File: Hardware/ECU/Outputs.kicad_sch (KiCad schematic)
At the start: 25 parts, among them IC2 ZXMS6006DT8, IC3 ZXMS6006DT8, IC4 ZXMS6006DT8

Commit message: modified:   .gitmodules 	modified:   Hardware/ECU/Comms.kicad_sch 	modified:   Hardware/ECU/ECU.kicad_pcb 	modified:   Hardware/ECU/ECU.kicad_pro 	modified:   Hardware/ECU/ECU.kicad_sch 	modified:   Hardware/ECU/Inputs.kicad_sch 	modified:   Hardware/ECU/Outputs.kicad_sch 	modified:   Hardware/ECU/fp-info-cache 	modified:   Hardware/ECU/fp-lib-table 	deleted:    docs/ECU info.url 	modified:   tune/Hayabusa-R1/CurrentTune.msq 	modified:   tune/Hayabusa-R1/projectCfg/project.properties 	modified:   tune/Hayabusa-R1/projectCfg/project.properties.bkup 	Hardware/ECU/ECU-backups/ECU-2024-11-07_084642.zip 	Hardware/ECU/ECU-backups/ECU-2024-11-07_091524.zip 	Hardware/ECU/ECU-backups/ECU-2024-11-07_094217.zip 	Hardware/ECU/ECU-backups/ECU-2024-11-07_120300.zip 	Hardware/ECU/ECU-backups/ECU-2024-11-08_085235.zip 	Hardware/ECU/ECU-backups/ECU-2024-11-08_091401.zip 	Hardware/ECU/ECU-backups/ECU-2024-11-08_103901.zip 	Hardware/ECU/docs/ 	Hardware/ECU/lib/2999/ 	Hardware/ECU/lib/IC_Automotive/IC_Automotive.pretty/BAT_2999.kicad_mod 	Hardware/ECU/lib/IC_Automotive/IC_Automotive.pretty/ZXMS6006DT8TA.kicad_mod 	Hardware/ECU/lib/ZXMS6006DT8TA/ 	Hardware/ECU/lib/teensy_library/ 	Hardware/ECU/output.pdf 	Hardware/ECU/report.txt 	docs/Speeduino_manual.pdf 	docs/Speeduino_manual.pdf:Zone.Identifier 	tune/Hayabusa-R1/dashboard/lambdaTable1Map.dash 	tune/Hayabusa-R1/dashboard/stagingMap.dash 	tune/TunerStudioAppDebug.txt
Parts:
- IC2, IC3, IC4: footprint IC_Automotive:Diodes_SM8 -> ZXMS6006DT8TA:SOT153P700X170-8N
- R53, R54, R55, R56, R58, R59, R60, R61, R62, R63, R64, R65: footprint Resistor_SMD:R_0805_2012Metric_Pad1.15x1.40mm_HandSolder -> Resistor_SMD:R_0805_2012Metric_Pad1.20x1.40mm_HandSolder
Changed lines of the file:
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@@
 			)
 		)
-		(property "Footprint" "Resistor_SMD:R_0805_2012Metric_Pad1.15x1.40mm_HandSolder"
+		(property "Footprint" "Resistor_SMD:R_0805_2012Metric_Pad1.20x1.40mm_HandSolder"
 			(at 194.818 110.49 90)
 			(effects
@@
 			)
 		)
-		(property "Footprint" "Resistor_SMD:R_0805_2012Metric_Pad1.15x1.40mm_HandSolder"
+		(property "Footprint" "Resistor_SMD:R_0805_2012Metric_Pad1.20x1.40mm_HandSolder"
 			(at 186.69 116.332 90)
 			(effects
@@
 			)
 		)
-		(property "Footprint" "Resistor_SMD:R_0805_2012Metric_Pad1.15x1.40mm_HandSolder"
+		(property "Footprint" "Resistor_SMD:R_0805_2012Metric_Pad1.20x1.40mm_HandSolder"
 			(at 50.038 57.15 90)
 			(effects
@@
 			)
 		)
-		(property "Footprint" "Resistor_SMD:R_0805_2012Metric_Pad1.15x1.40mm_HandSolder"
+		(property "Footprint" "Resistor_SMD:R_0805_2012Metric_Pad1.20x1.40mm_HandSolder"
 			(at 194.818 130.81 90)
 			(effects
@@
 			)
 		)
-		(property "Footprint" "IC_Automotive:Diodes_SM8"
+		(property "Footprint" "ZXMS6006DT8TA:SOT153P700X170-8N"
 			(at 236.22 41.91 0)
 			(effects
@@
 			)
 		)
-		(property "Footprint" "Resistor_SMD:R_0805_2012Metric_Pad1.15x1.40mm_HandSolder"
+		(property "Footprint" "Resistor_SMD:R_0805_2012Metric_Pad1.20x1.40mm_HandSolder"
 			(at 41.91 42.672 90)
 			(effects
@@
 			)
 		)
-		(property "Footprint" "Resistor_SMD:R_0805_2012Metric_Pad1.15x1.40mm_HandSolder"
+		(property "Footprint" "Resistor_SMD:R_0805_2012Metric_Pad1.20x1.40mm_HandSolder"
 			(at 196.088 36.83 90)
 			(effects
@@
 			)
 		)
-		(property "Footprint" "IC_Automotive:Diodes_SM8"
+		(property "Footprint" "ZXMS6006DT8TA:SOT153P700X170-8N"
 			(at 234.95 115.57 0)
 			(effects
@@
 			)
 		)
-		(property "Footprint" "Resistor_SMD:R_0805_2012Metric_Pad1.15x1.40mm_HandSolder"
+		(property "Footprint" "Resistor_SMD:R_0805_2012Metric_Pad1.20x1.40mm_HandSolder"
 			(at 41.91 47.752 90)
 			(effects
@@
 			)
 		)
-		(property "Footprint" "Resistor_SMD:R_0805_2012Metric_Pad1.15x1.40mm_HandSolder"
+		(property "Footprint" "Resistor_SMD:R_0805_2012Metric_Pad1.20x1.40mm_HandSolder"
 			(at 187.96 42.672 90)
 			(effects
@@
 			)
 		)
-		(property "Footprint" "Resistor_SMD:R_0805_2012Metric_Pad1.15x1.40mm_HandSolder"
+		(property "Footprint" "Resistor_SMD:R_0805_2012Metric_Pad1.20x1.40mm_HandSolder"
 			(at 50.038 36.83 90)
 			(effects
@@
 			)
 		)
-		(property "Footprint" "IC_Automotive:Diodes_SM8"
+		(property "Footprint" "ZXMS6006DT8TA:SOT153P700X170-8N"
 			(at 90.17 41.91 0)
 			(effects
@@
 			)
 		)
-		(property "Footprint" "Resistor_SMD:R_0805_2012Metric_Pad1.15x1.40mm_HandSolder"
+		(property "Footprint" "Resistor_SMD:R_0805_2012Metric_Pad1.20x1.40mm_HandSolder"
 			(at 186.69 121.412 90)
 			(effects
@@
 			)
 		)
-		(property "Footprint" "Resistor_SMD:R_0805_2012Metric_Pad1.15x1.40mm_HandSolder"
+		(property "Footprint" "Resistor_SMD:R_0805_2012Metric_Pad1.20x1.40mm_HandSolder"
 			(at 196.088 57.15 90)
 			(effects
@@
 			)
 		)
-		(property "Footprint" "Resistor_SMD:R_0805_2012Metric_Pad1.15x1.40mm_HandSolder"
+		(property "Footprint" "Resistor_SMD:R_0805_2012Metric_Pad1.20x1.40mm_HandSolder"
 			(at 187.96 47.752 90)
 			(effects

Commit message: PCB
Platine Vernetzt
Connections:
- net GND: now also R55.1; no longer R55.2
- net at IC2.1 (INPUT_1), R53.1: now also R55.2; no longer R55.1
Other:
- moved on the sheet: R55
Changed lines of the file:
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@@
 	(symbol
 		(lib_id "Device:R")
-		(at 48.26 36.83 180)
+		(at 48.26 36.83 0)
+		(mirror y)
 		(unit 1)
 		(exclude_from_sim no)
@@
 		(dnp no)
 		(property "Reference" "R55"
-			(at 50.038 35.6616 0)
+			(at 50.038 37.9984 0)
 			(effects
 				(font
@@
 		)
 		(property "Value" "100k"
-			(at 50.038 37.973 0)
+			(at 50.038 35.687 0)
 			(effects
 				(font
@@
 		)
 		(property "Manufacturer_Name" "Yageo"
-			(at 99.06 1.27 0)
+			(at 99.06 72.39 0)
 			(effects
 				(font
@@
 		)
 		(property "Manufacturer_Part_Number" "RC0805FR-07100KL"
-			(at 99.06 1.27 0)
+			(at 99.06 72.39 0)
 			(effects
 				(font
@@
 		)
 		(property "URL" "https://www.digikey.com/product-detail/en/yageo/RC0805FR-07100KL/311-100KCRCT-ND/730491"
-			(at 99.06 1.27 0)
+			(at 99.06 72.39 0)
 			(effects
 				(font
@@
 		)
 		(property "Digikey Part Number" "311-100KCRCT-ND"
-			(at 99.06 1.27 0)
+			(at 99.06 72.39 0)
 			(effects
 				(font

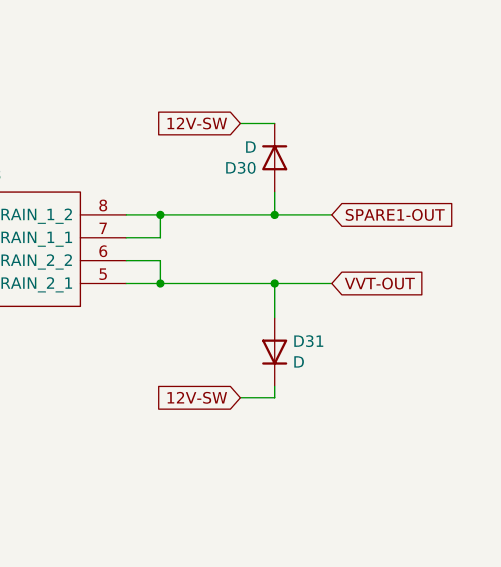
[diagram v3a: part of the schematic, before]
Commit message: PCB v0.2
leiterbahndicke updated
Clutch input rework
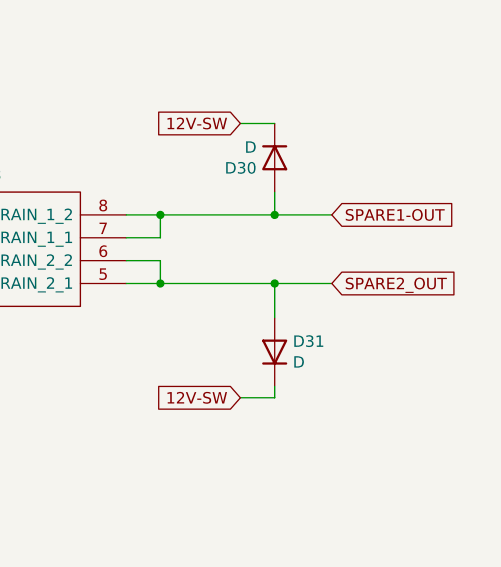
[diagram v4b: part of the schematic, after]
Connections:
- net VVT-OUT renamed SPARE2_OUT
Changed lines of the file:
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@@
 		)
 		(property "Intersheetrefs" "${INTERSHEET_REFS}"
-			(at 276.2692 118.11 0)
+			(at 277.0028 118.11 0)
 			(effects
 				(font
@@
 		)
 	)
-	(global_label "VVT-OUT"
+	(global_label "SPARE2_OUT"
 		(shape input)
 		(at 261.62 125.73 0)
@@
 		)
 		(property "Intersheetrefs" "${INTERSHEET_REFS}"
-			(at 272.2174 125.73 0)
-			(effects
-				(font
+			(at 276.398 125.73 0)
+			(effects
+				(font
